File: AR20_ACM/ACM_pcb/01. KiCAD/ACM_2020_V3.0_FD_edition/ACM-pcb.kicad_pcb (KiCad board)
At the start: 2 copper layers, 19.8 x 28 mm, 33 parts, among them J1 TC2030-MCP-NL, P1 Conn_02x15_Odd_Even, Q1 Q_PMOS_DMP3099L-13, U1 ATmega328P-AU, U2 MCP2542FDxMF, U3 NCV890430MW50TXG, U4 MCP2517FD-xSL, Y1 16.0Mhz, Y2 20.0 Mhz

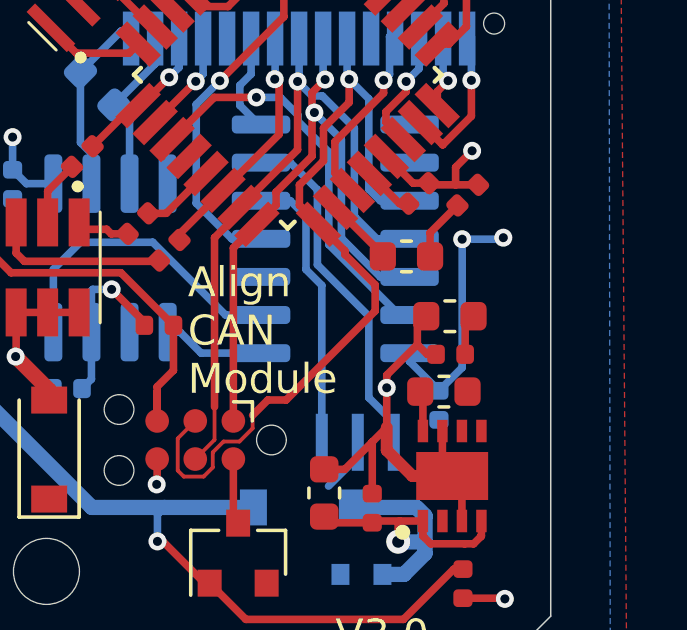
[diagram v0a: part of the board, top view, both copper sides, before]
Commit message: Added 10k resistor between VDD and CS
As requested by the ACAN library I added a 10k resistor between VDD and CS
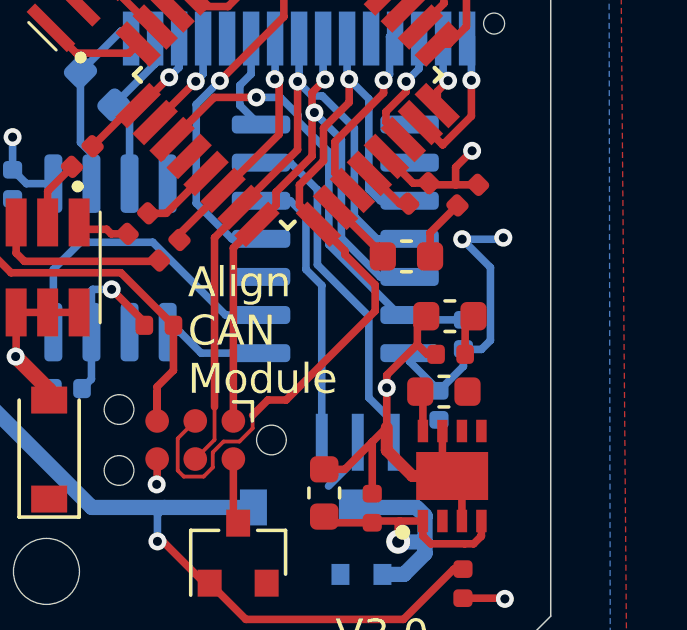
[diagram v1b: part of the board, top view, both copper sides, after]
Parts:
- added R6: 10K Ohm, Resistor_SMD:R_0402_1005Metric, B.Cu at (79.9, 81.1)
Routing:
- net /CAN_CS: track 13.8 -> 15.7 mm
- net +5V: track 28.3 -> 29.5 mm

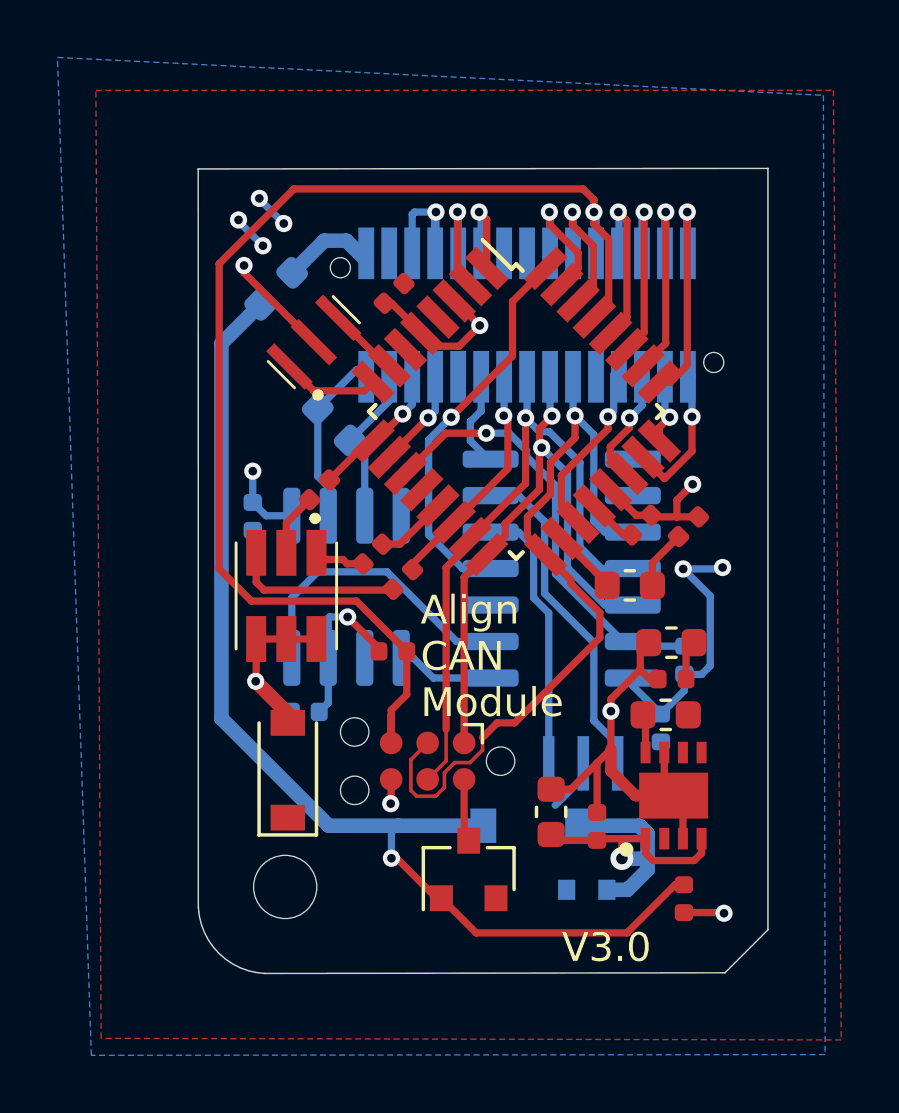
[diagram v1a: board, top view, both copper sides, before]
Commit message: Updated 10k resistor position and version
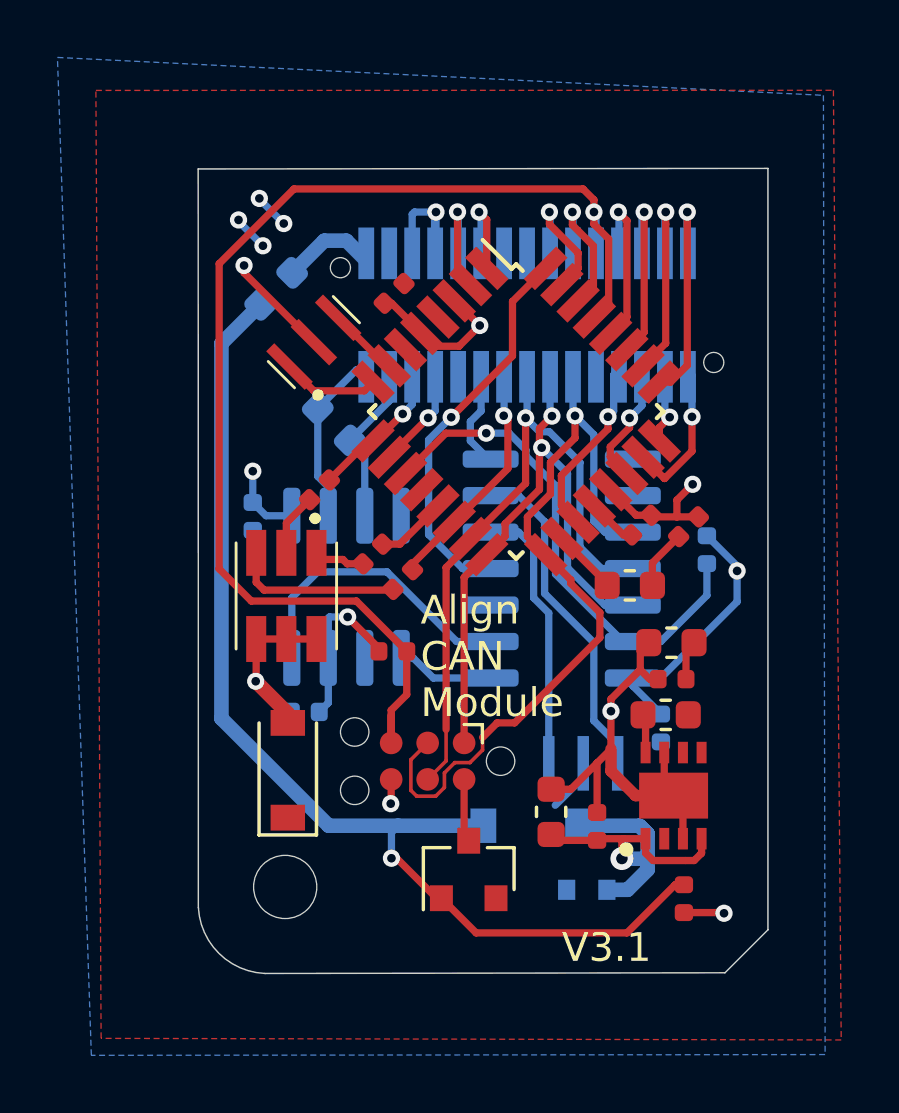
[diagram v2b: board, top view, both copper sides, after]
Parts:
- moved R6 3.92 mm to (80.7, 77.3), turned to 270 degrees
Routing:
- net /CAN_CS: track 15.7 -> 18.4 mm
- net +5V: track 29.5 -> 29.0 mm, vias 9 -> 8
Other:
- board text added: "V3.1"
- board text removed: "V3.0"
